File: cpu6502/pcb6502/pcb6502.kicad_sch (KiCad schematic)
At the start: 38 parts, among them J1 Power, J2 RS232, J3 VIA PA, J4 VIA PB, J5 Ext RST, J6 Address, J7 Data, J8 CPU, J9 Interrupt Enable, SW1 Reset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

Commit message: forgot to save previous
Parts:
- removed J9: Interrupt Enable, Connector_PinHeader_2.54mm:PinHeader_2x06_P2.54mm_Vertical, symbol Connector_Generic:Conn_02x06_Odd_Even
- added SW2: IRQ Enable, Button_Switch_THT:SW_DIP_SPSTx06_Slide_6.7x16.8mm_W7.62mm_P2.54mm_LowProfile, symbol Switch:SW_DIP_x06
- J8: footprint (none) -> Connector_PinHeader_2.54mm:PinHeader_2x04_P2.54mm_Vertical
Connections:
- net +5V: now also SW2.12, SW2.7
- net ACIAIRQ: now also SW2.11
- net ExtIRQ: now also SW2.9
- net ExtNMI: now also SW2.8
- net IRQ: now also SW2.1, SW2.2, SW2.3, SW2.4
- net NMI: now also SW2.5, SW2.6; no longer J8.7 (Pin_7)
- net VIAIRQ: now also SW2.10
- no-connect marks 25 -> 26
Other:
- moved on the sheet: J6, J7

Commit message: PCB: Add RS232 RCV LED, get pours connected, CODE: checkpoint
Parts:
- removed J5: Ext RST, Connector_PinHeader_2.54mm:PinHeader_2x01_P2.54mm_Vertical, symbol Connector_Generic:Conn_02x01
- added D4: RCV LED, LED_THT:LED_D3.0mm, symbol Device:LED
- added R1: 220, Resistor_THT:R_Axial_DIN0207_L6.3mm_D2.5mm_P2.54mm_Vertical, symbol Device:R
- U6: footprint Package_TO_SOT_THT:TO-220F-3_Horizontal_TabUp -> Package_TO_SOT_THT:TO-220-3_Horizontal_TabDown
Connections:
- net GND: now also SW1.2, R1.2
- net RST: now also SW1.1, U9.1 (RST); no longer SW1.2
- net at J2.3, U8.13 (R1IN): now also D4.2 (A)
- new net: D4.1 (K), R1.1
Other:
- moved on the sheet: SW1
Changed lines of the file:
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@@
     (title "Chris G 6502")
   )
-  (junction (at 142.24 146.05) (diameter 0) (color 0 0 0 0)
-  )
   (junction (at 255.27 46.99) (diameter 0) (color 0 0 0 0)
   )
@@
   (junction (at 149.86 153.67) (diameter 0) (color 0 0 0 0)
   )
+  (junction (at 243.84 147.32) (diameter 0) (color 0 0 0 0)
+  )
   (junction (at 91.44 102.87) (diameter 0) (color 0 0 0 0)
   )
   (junction (at 69.85 123.19) (diameter 0) (color 0 0 0 0)
   )
-  (junction (at 129.54 146.05) (diameter 0) (color 0 0 0 0)
-  )
   (junction (at 255.27 49.53) (diameter 0) (color 0 0 0 0)
   )
@@
   (junction (at 156.21 161.29) (diameter 0) (color 0 0 0 0)
   )
+  (junction (at 130.81 146.05) (diameter 0) (color 0 0 0 0)
+  )
   (no_connect (at 240.03 152.4))
   (no_connect (at 257.81 138.43))
@@
     (stroke (width 0) (type default))
   )
-  (wire (pts (xy 129.54 137.16) (xy 129.54 146.05))
-    (stroke (width 0) (type default))
-  )
   (wire (pts (xy 62.23 86.36) (xy 59.69 86.36))
     (stroke (width 0) (type default))
@@
     (stroke (width 0) (type default))
   )
+  (wire (pts (xy 252.73 160.02) (xy 256.54 160.02))
+    (stroke (width 0) (type default))
+  )
   (wire (pts (xy 162.56 101.6) (xy 167.64 101.6))
     (stroke (width 0) (type default))
@@
     (stroke (width 0) (type default))
   )
+  (wire (pts (xy 243.84 160.02) (xy 245.11 160.02))
+    (stroke (width 0) (type default))
+  )
   (wire (pts (xy 168.91 138.43) (xy 168.91 135.89))
     (stroke (width 0) (type default))
@@
     (stroke (width 0) (type default))
   )
-  (wire (pts (xy 142.24 146.05) (xy 142.24 137.16))
-    (stroke (width 0) (type default))
-  )
   (wire (pts (xy 62.23 93.98) (xy 59.69 93.98))
     (stroke (width 0) (type default))
@@
     (stroke (width 0) (type default))
   )
+  (wire (pts (xy 130.81 146.05) (xy 139.7 146.05))
+    (stroke (width 0) (type default))
+  )
   (wire (pts (xy 121.92 91.44) (xy 121.92 86.36))
     (stroke (width 0) (type default))
@@
     (stroke (width 0) (type default))
   )
+  (wire (pts (xy 127 146.05) (xy 130.81 146.05))
+    (stroke (width 0) (type default))
+  )
   (wire (pts (xy 41.91 161.29) (xy 44.45 161.29))
     (stroke (width 0) (type default))
@@
     (stroke (width 0) (type default))
   )
-  (wire (pts (xy 139.7 146.05) (xy 142.24 146.05))
-    (stroke (width 0) (type default))
-  )
   (wire (pts (xy 59.69 66.04) (xy 62.23 66.04))
     (stroke (width 0) (type default))
@@
     (stroke (width 0) (type default))
   )
-  (wire (pts (xy 127 146.05) (xy 129.54 146.05))
-    (stroke (width 0) (type default))
-  )
   (wire (pts (xy 270.51 54.61) (xy 273.05 54.61))
     (stroke (width 0) (type default))
@@
     (stroke (width 0) (type default))
   )
+  (wire (pts (xy 130.81 146.05) (xy 130.81 152.4))
+    (stroke (width 0) (type default))
+  )
   (wire (pts (xy 33.02 58.42) (xy 39.37 58.42))
     (stroke (width 0) (type default))
@@
     (stroke (width 0) (type default))
   )
+  (wire (pts (xy 243.84 147.32) (xy 243.84 160.02))
+    (stroke (width 0) (type default))
+  )
   (wire (pts (xy 146.05 53.34) (xy 143.51 53.34))
     (stroke (width 0) (type default))
@@
     (stroke (width 0) (type default))
   )
-  (wire (pts (xy 142.24 146.05) (xy 143.51 146.05))
-    (stroke (width 0) (type default))
-  )
   (wire (pts (xy 118.11 53.34) (xy 123.19 53.34))
     (stroke (width 0) (type default))
@@
     (effects (font (size 1.27 1.27)) (justify left bottom))
   )
-  (label "RST" (at 143.51 146.05 0) (fields_autoplaced)
+  (label "RST" (at 139.7 146.05 0) (fields_autoplaced)
     (effects (font (size 1.27 1.27)) (justify left bottom))
   )
@@
     )
   )
-  (symbol (lib_id "Switch:SW_Push") (at 134.62 146.05 0) (unit 1)
+  (symbol (lib_id "Switch:SW_Push") (at 135.89 152.4 0) (unit 1)
     (in_bom yes) (on_board yes) (dnp no)
-    (property "Reference" "SW1" (at 134.62 148.59 0)
+    (property "Reference" "SW1" (at 135.89 154.94 0)
       (effects (font (size 1.27 1.27)))
     )
-    (property "Value" "Reset" (at 134.62 142.24 0)
+    (property "Value" "Reset" (at 135.89 148.59 0)
       (effects (font (size 1.27 1.27)))
     )
-    (property "Footprint" "Button_Switch_THT:SW_TH_Tactile_Omron_B3F-10xx" (at 134.62 140.97 0)
+    (property "Footprint" "Button_Switch_THT:SW_TH_Tactile_Omron_B3F-10xx" (at 135.89 147.32 0)
       (effects (font (size 1.27 1.27)) hide)
     )
-    (property "Datasheet" "~" (at 134.62 140.97 0)
+    (property "Datasheet" "~" (at 135.89 147.32 0)
       (effects (font (size 1.27 1.27)) hide)
     )
@@
     )
   )
+  (symbol (lib_id "power:GND") (at 140.97 152.4 90) (unit 1)
+    (in_bom yes) (on_board yes) (dnp no)
+    (property "Reference" "#PWR045" (at 147.32 152.4 0)
+      (effects (font (size 1.27 1.27)) hide)
+    )
+    (property "Value" "GND" (at 144.78 152.4 0)
+      (effects (font (size 1.27 1.27)))
+    )
+    (property "Footprint" "" (at 140.97 152.4 0)
+      (effects (font (size 1.27 1.27)) hide)
+    )
+    (property "Datasheet" "" (at 140.97 152.4 0)
+      (effects (font (size 1.27 1.27)) hide)
+    )
+    (pin "1")
+    (instances
+      (project "pcb6502"
+        (path "/aae31785-fe90-4323-8d48-945b25f108ea"
+          (reference "#PWR045") (unit 1)
+        )
+      )
+    )
+  )
   (symbol (lib_id "power:+5V") (at 25.4 176.53 90) (unit 1)
     (in_bom yes) (on_board yes) (dnp no) (fields_autoplaced)
@@
     )
   )
+  (symbol (lib_id "Device:LED") (at 248.92 160.02 180) (unit 1)
+    (in_bom yes) (on_board yes) (dnp no)
+    (property "Reference" "D4" (at 246.38 156.21 0)
+      (effects (font (size 1.27 1.27)) (justify right))
+    )
+    (property "Value" "RCV LED" (at 243.84 163.83 0)
+      (effects (font (size 1.27 1.27)) (justify right))
+    )
+    (property "Footprint" "LED_THT:LED_D3.0mm" (at 248.92 160.02 0)
+      (effects (font (size 1.27 1.27)) hide)
+    )
+    (property "Datasheet" "~" (at 248.92 160.02 0)
+      (effects (font (size 1.27 1.27)) hide)
+    )
+    (pin "1")
+    (pin "2")
+    (instances
+      (project "pcb6502"
+        (path "/aae31785-fe90-4323-8d48-945b25f108ea"
+          (reference "D4") (unit 1)
+        )
+      )
+    )
+  )
   (symbol (lib_id "power:GND") (at 102.87 26.67 0) (unit 1)
     (in_bom yes) (on_board yes) (dnp no)
@@
       (effects (font (size 1.27 1.27)))
     )
-    (property "Footprint" "Package_TO_SOT_THT:TO-220F-3_Horizontal_TabUp" (at 116.205 176.53 0)
+    (property "Footprint" "Package_TO_SOT_THT:TO-220-3_Horizontal_TabDown" (at 116.205 176.53 0)
       (effects (font (size 1.27 1.27) italic) (justify left) hide)
     )
@@
     )
   )
+  (symbol (lib_id "power:GND") (at 264.16 160.02 90) (unit 1)
+    (in_bom yes) (on_board yes) (dnp no)
+    (property "Reference" "#PWR046" (at 270.51 160.02 0)
+      (effects (font (size 1.27 1.27)) hide)
+    )
+    (property "Value" "GND" (at 267.97 160.02 0)
+      (effects (font (size 1.27 1.27)))
+    )
+    (property "Footprint" "" (at 264.16 160.02 0)
+      (effects (font (size 1.27 1.27)) hide)
+    )
+    (property "Datasheet" "" (at 264.16 160.02 0)
+      (effects (font (size 1.27 1.27)) hide)
+    )
+    (pin "1")
+    (instances
+      (project "pcb6502"
+        (path "/aae31785-fe90-4323-8d48-945b25f108ea"
+          (reference "#PWR046") (unit 1)
+        )
+      )
+    )
+  )
   (symbol (lib_id "Mechanical:MountingHole_Pad") (at 102.87 24.13 0) (unit 1)
     (in_bom yes) (on_board yes) (dnp no) (fields_autoplaced)
@@
     )
   )
-  (symbol (lib_id "Connector_Generic:Conn_02x01") (at 134.62 137.16 0) (unit 1)
-    (in_bom yes) (on_board yes) (dnp no) (fields_autoplaced)
-    (property "Reference" "J5" (at 135.89 130.81 0)
-      (effects (font (size 1.27 1.27)))
-    )
-    (property "Value" "Ext RST" (at 135.89 133.35 0)
-      (effects (font (size 1.27 1.27)))
-    )
-    (property "Footprint" "Connector_PinHeader_2.54mm:PinHeader_2x01_P2.54mm_Vertical" (at 134.62 137.16 0)
-      (effects (font (size 1.27 1.27)) hide)
-    )
-    (property "Datasheet" "~" (at 134.62 137.16 0)
-      (effects (font (size 1.27 1.27)) hide)
-    )
-    (pin "1")
-    (pin "2")
-    (instances
-      (project "pcb6502"
-        (path "/aae31785-fe90-4323-8d48-945b25f108ea"
-          (reference "J5") (unit 1)
-        )
-      )
-    )
-  )
   (symbol (lib_id "power:+5V") (at 273.05 58.42 180) (unit 1)
     (in_bom yes) (on_board yes) (dnp no)
@@
         )
       )
+    )
+  )
+  (symbol (lib_id "Device:R") (at 260.35 160.02 90) (unit 1)
+    (in_bom yes) (on_board yes) (dnp no)
+    (property "Reference" "R1" (at 260.35 157.48 90)
+      (effects (font (size 1.27 1.27)))
+    )
+    (property "Value" "220" (at 260.35 160.02 90)
+      (effects (font (size 1.27 1.27)))
+    )
+    (property "Footprint" "Resistor_THT:R_Axial_DIN0207_L6.3mm_D2.5mm_P2.54mm_Vertical" (at 260.35 161.798 90)
+      (effects (font (size 1.27 1.27)) hide)
+    )
+    (property "Datasheet" "~" (at 260.35 160.02 0)
+      (effects (font (size 1.27 1.27)) hide)
+    )
+    (pin "1")
+    (pin "2")
+    (instances
+      (project "pcb6502"
+        (path "/aae31785-fe90-4323-8d48-945b25f108ea"
+          (reference "R1") (unit 1)
+        )
+      )

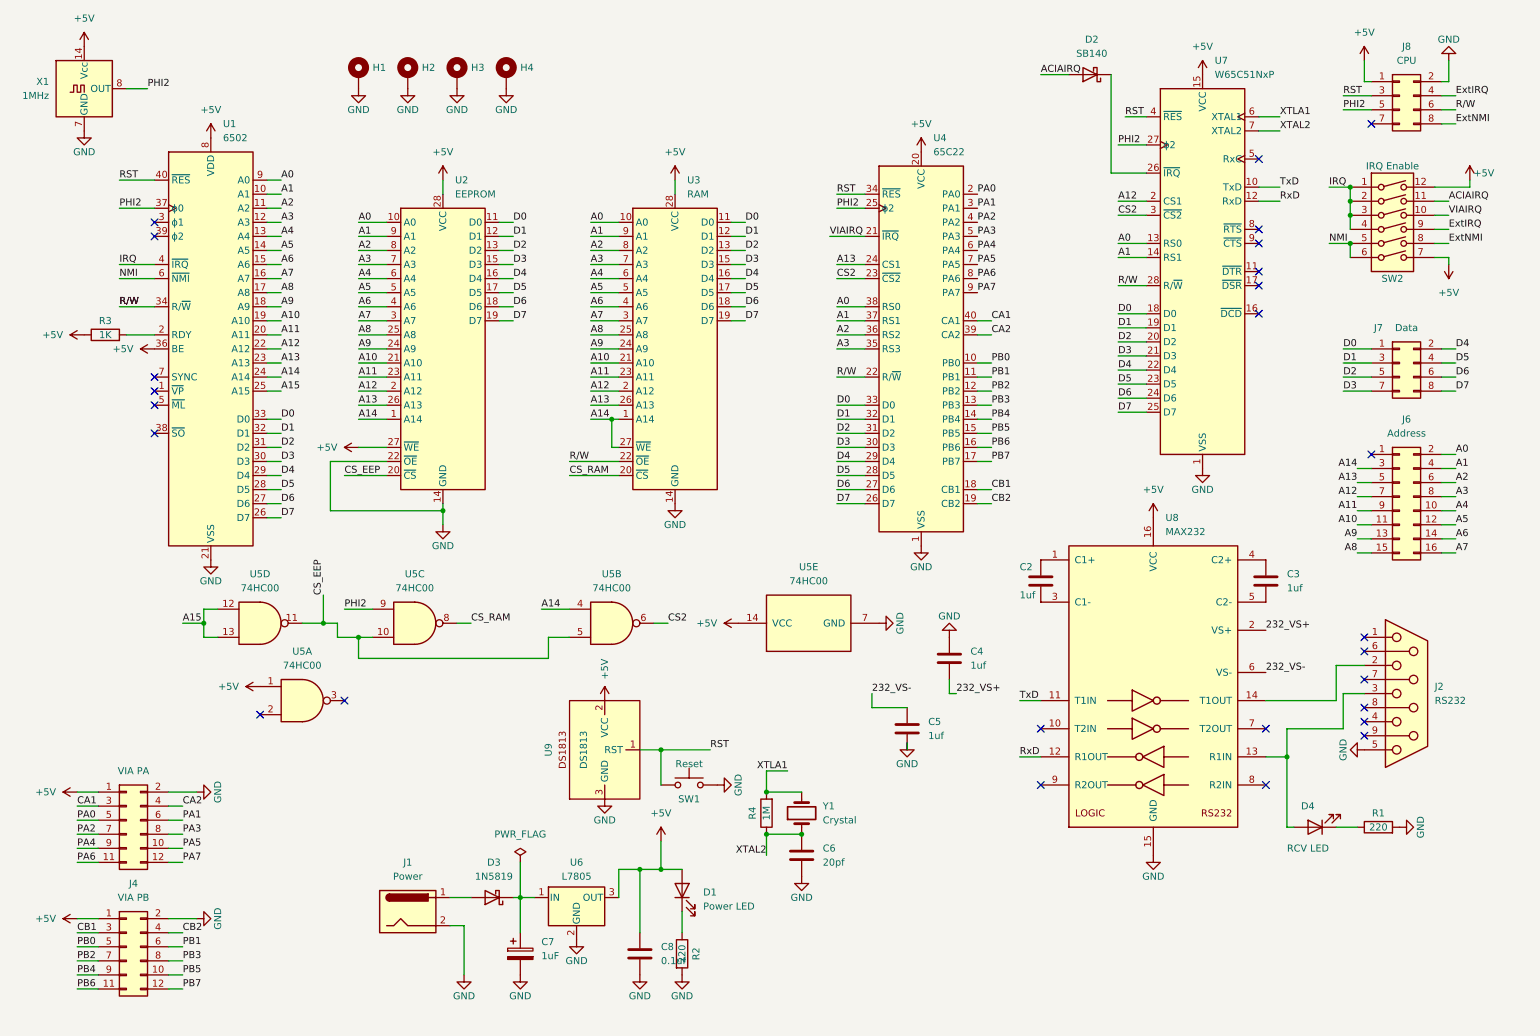
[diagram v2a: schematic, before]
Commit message: update PCB with debug button, other cleanup, add Wozmon to cgOS and get it working!
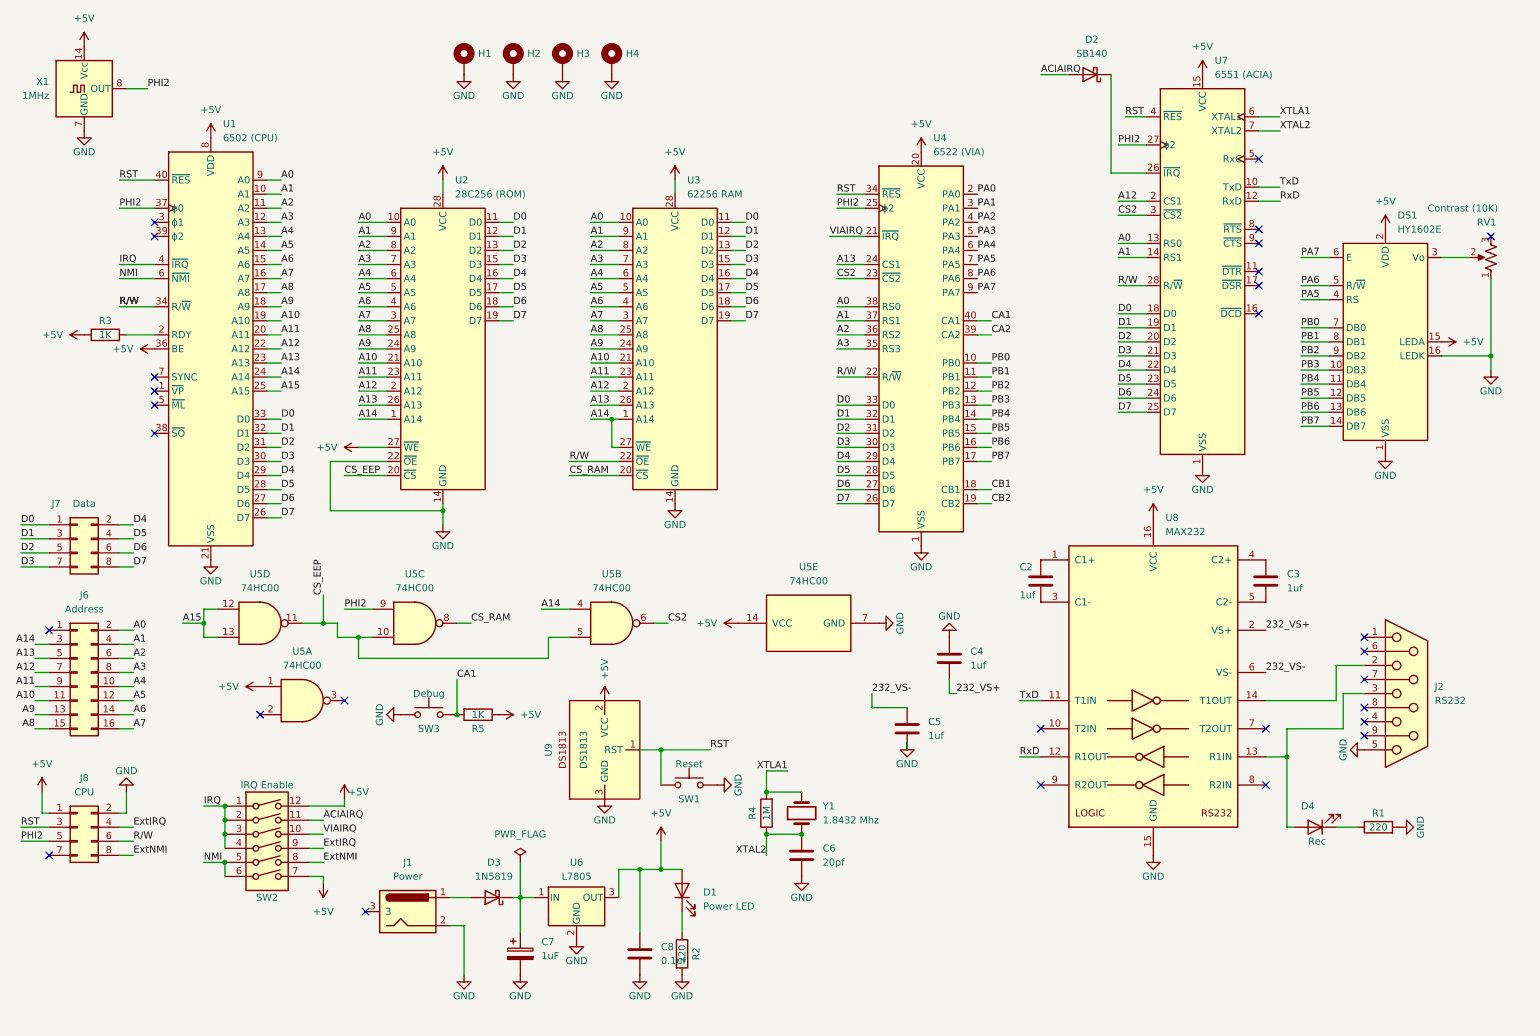
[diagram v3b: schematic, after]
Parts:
- removed J3: VIA PA, Connector_PinHeader_2.54mm:PinHeader_2x06_P2.54mm_Vertical, symbol Connector_Generic:Conn_02x06_Odd_Even
- removed J4: VIA PB, Connector_PinHeader_2.54mm:PinHeader_2x06_P2.54mm_Vertical, symbol Connector_Generic:Conn_02x06_Odd_Even
- added DS1: HY1602E, Display:WC1602A, symbol Display_Character:HY1602E
- added R5: 1K, Resistor_THT:R_Axial_DIN0204_L3.6mm_D1.6mm_P2.54mm_Vertical, symbol Device:R
- added RV1: Contrast (10K), Potentiometer_THT:Potentiometer_Bourns_3386P_Vertical, symbol Device:R_Potentiometer_US
- added SW3: Debug, Button_Switch_THT:SW_TH_Tactile_Omron_B3F-10xx, symbol Switch:SW_Push
- D4: value RCV LED -> Rec
- U1: value 6502 -> 6502 (CPU)
- U2: value EEPROM -> 28C256 (ROM)
- U3: value RAM -> 62256 RAM
- U4: value 65C22 -> 6522 (VIA)
- U7: value W65C51NxP -> 6551 (ACIA)
- Y1: value Crystal -> 1.8432 Mhz
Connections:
- net +5V: now also DS1.15 (LEDA), DS1.2 (VDD), R5.1
- net CA1: now also R5.2, SW3.2
- net GND: now also DS1.1 (VSS), DS1.16 (LEDK), RV1.1, SW3.1
- net PA5: now also DS1.4 (RS)
- net PA6: now also DS1.5 (R/~{W})
- net PA7: now also DS1.6 (E)
- net PB0: now also DS1.7 (DB0)
- net PB1: now also DS1.8 (DB1)
- net PB2: now also DS1.9 (DB2)
- net PB3: now also DS1.10 (DB3)
- net PB4: now also DS1.11 (DB4)
- net PB5: now also DS1.12 (DB5)
- net PB6: now also DS1.13 (DB6)
- net PB7: now also DS1.14 (DB7)
- new net: DS1.3 (Vo), RV1.2
- no-connect marks 26 -> 28
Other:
- moved on the sheet: H1, H2, H3, H4, J6, J7, J8, SW2

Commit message: checkpoint, most significantly OS works!!
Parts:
- added D5: Activity, LED_THT:LED_D5.0mm, symbol Device:LED
- added D6: 1N5819, Diode_THT:D_DO-41_SOD81_P10.16mm_Horizontal, symbol Diode:1N5819
- added J3: 5v Power, TerminalBlock_TE-Connectivity:TerminalBlock_TE_282834-2_1x02_P2.54mm_Horizontal, symbol Connector:Screw_Terminal_01x02
- added R6: 220, Resistor_THT:R_Axial_DIN0204_L3.6mm_D1.6mm_P7.62mm_Horizontal, symbol Device:R
- D1: value Power LED -> Power
- D4: value Rec -> Receive; footprint LED_THT:LED_D3.0mm -> LED_THT:LED_D5.0mm
- J2: footprint Connector_Dsub:DSUB-9_Female_Horizontal_P2.77x2.54mm_EdgePinOffset9.40mm -> Connector_Dsub:DSUB-9_Male_Horizontal_P2.77x2.84mm_EdgePinOffset4.94mm_Housed_MountingHolesOffset7.48mm; symbol Connector:DE9_Receptacle -> Connector:DE9_Receptacle_MountingHoles
- R1: footprint Resistor_THT:R_Axial_DIN0207_L6.3mm_D2.5mm_P2.54mm_Vertical -> Resistor_THT:R_Axial_DIN0204_L3.6mm_D1.6mm_P7.62mm_Horizontal
- R5: footprint Resistor_THT:R_Axial_DIN0204_L3.6mm_D1.6mm_P2.54mm_Vertical -> Resistor_THT:R_Axial_DIN0204_L3.6mm_D1.6mm_P7.62mm_Horizontal
- U3: value 62256 RAM -> 62256 (RAM)
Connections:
- net +5V: now also D6.1 (K)
- net GND: now also J2.0 (PAD), J3.1 (Pin_1), R6.2
- net PA0: now also D5.2 (A)
- net CA2: no longer names the net of U4.39 (CA2)
- net CB1: no longer names the net of U4.18 (CB1)
- net CB2: no longer names the net of U4.19 (CB2)
- net PA1: no longer names the net of U4.3 (PA1)
- net PA2: no longer names the net of U4.4 (PA2)
- net PA3: no longer names the net of U4.5 (PA3)
- net PA4: no longer names the net of U4.6 (PA4)
- new net: D6.2 (A), J3.2 (Pin_2)
- new net: D5.1 (K), R6.1
- no-connect marks 28 -> 35
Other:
- moved on the sheet: C6, C7, C8, D1, D3, J1, R2, R4, SW1, SW2, U6, U9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
